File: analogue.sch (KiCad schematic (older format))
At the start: 0 parts

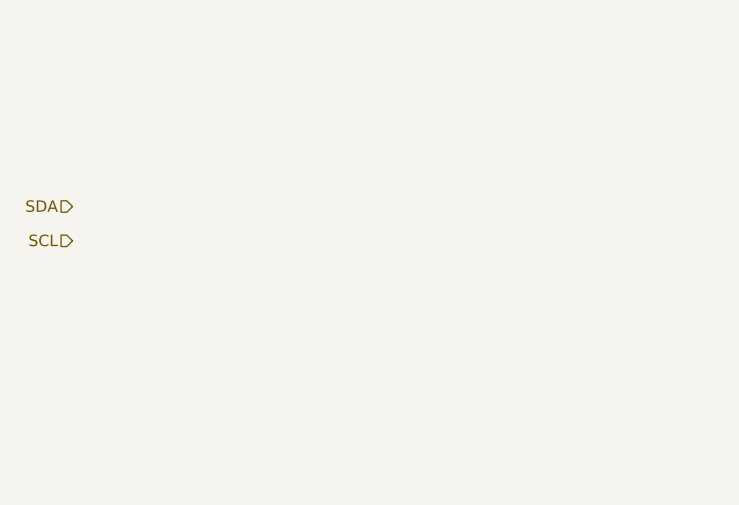
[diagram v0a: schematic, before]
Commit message: made ads1219 symbol
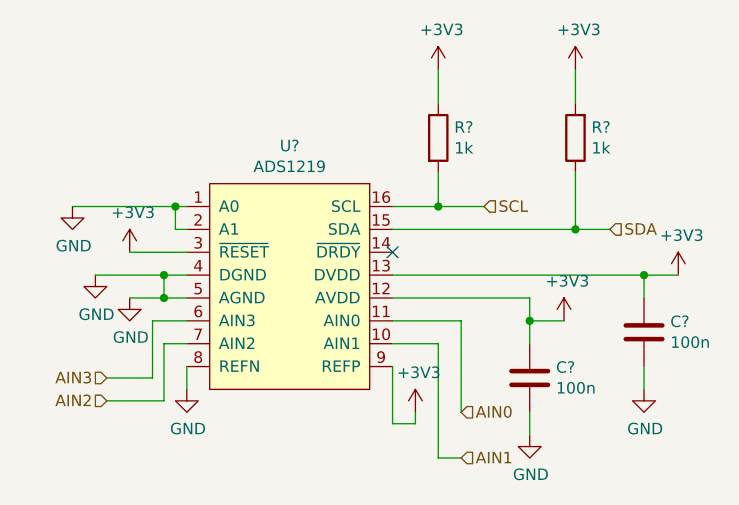
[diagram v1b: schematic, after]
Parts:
- added C? (x2): 100n, symbol Device:C
- added R? (x2): 1k, symbol Device:R
- added U?: ADS1219, symbol daq-hardware-cache:ADS1219
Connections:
- net SCL: now also R?.2, U?.16 (SCL)
- net SDA: now also R?.1, U?.15 (SDA)
- new net +3V3: C?.1, C?.2, R?.1, R?.2, U?.12 (AVDD), U?.13 (DVDD), U?.3 (~RESET), U?.9 (REFP)
- new net AIN0: U?.11 (AIN0)
- new net AIN1: U?.10 (AIN1)
- new net AIN2: U?.7 (AIN2)
- new net AIN3: U?.6 (AIN3)
- new net GND: C?.1, C?.2, U?.1 (A0), U?.2 (A1), U?.4 (DGND), U?.5 (AGND), U?.8 (REFN)
- no-connect marks 0 -> 1

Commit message: added analog input pins to main file
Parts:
- U?: symbol daq-hardware-cache:ADS1219 -> daq-hardware-rescue:ADS1219-daq-hardware-cache
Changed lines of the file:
@@
 EESchema Schematic File Version 4
-LIBS:analogue-cache
+LIBS:daq-hardware-cache
 EELAYER 30 0
 EELAYER END
 $Descr A4 11693 8268
 encoding utf-8
-Sheet 1 1
+Sheet 1 3
 Title ""
 Date ""
@@
 	4800 3850 4800 4100
 $Comp
-L daq-hardware-cache:ADS1219 U?
+L daq-hardware-rescue:ADS1219-daq-hardware-cache U?
 U 1 1 5DAAE850
 P 4350 3500
